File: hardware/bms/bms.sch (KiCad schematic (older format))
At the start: 172 parts

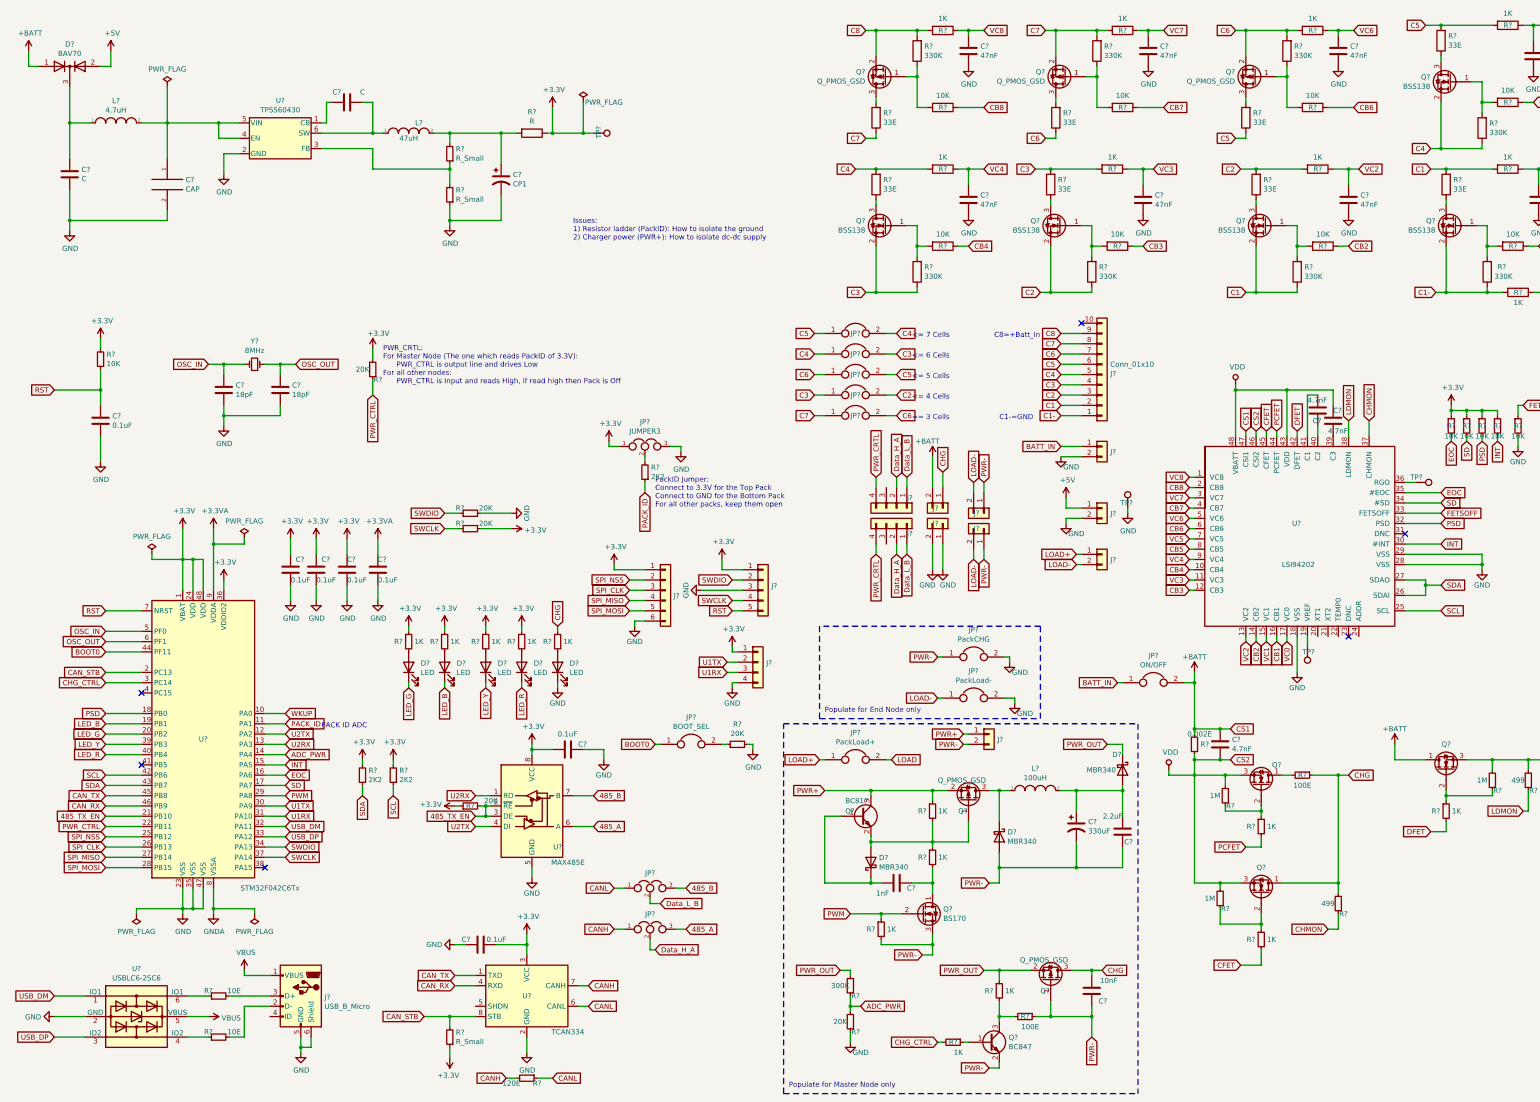
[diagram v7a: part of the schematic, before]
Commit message: added pack power management
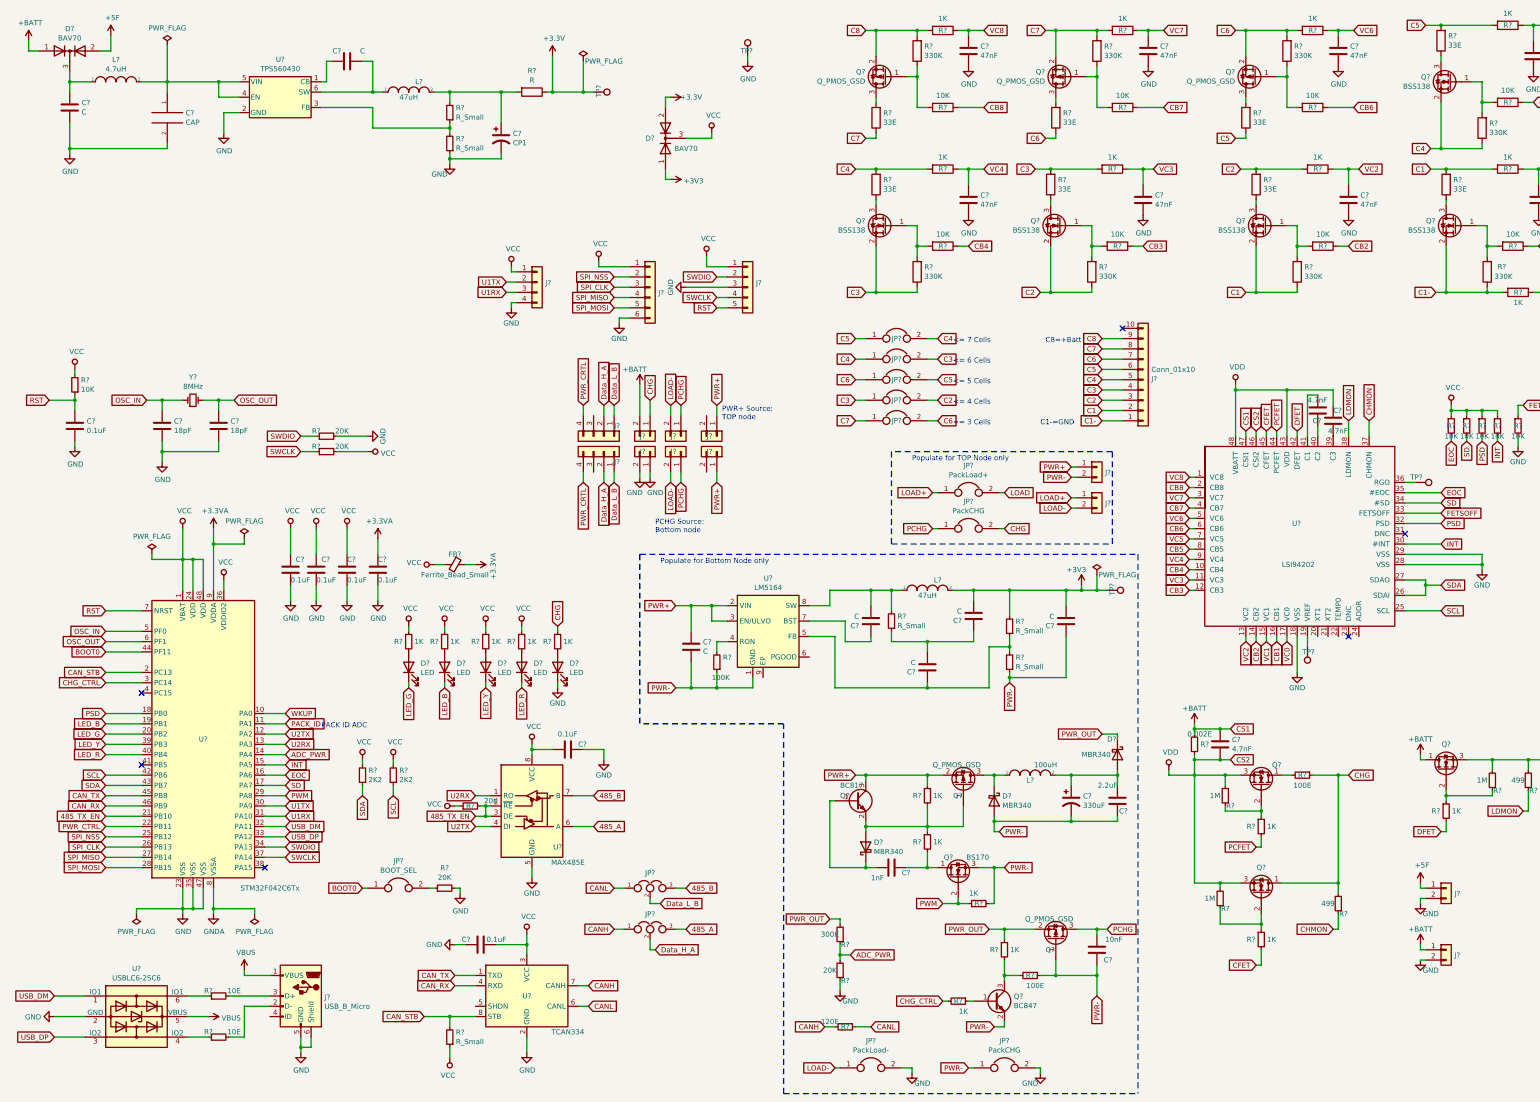
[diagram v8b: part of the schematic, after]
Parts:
- removed JP?: JUMPER3, symbol BMS:JUMPER3
- removed JP?: ON/OFF, symbol BMS:JUMPER
- removed R?: 2K2, Resistor_SMD:R_0603_1608Metric_Pad1.05x0.95mm_HandSolder, symbol Device:R_Small
- removed R?: 20K, Resistor_SMD:R_0603_1608Metric_Pad1.05x0.95mm_HandSolder, symbol Device:R_Small
- added C? (x5): C, Capacitor_SMD:C_0603_1608Metric_Pad1.05x0.95mm_HandSolder, symbol Device:C
- added D?: BAV70, Package_TO_SOT_SMD:SOT-23, symbol Diode:BAV70
- added FB?: Ferrite_Bead_Small, symbol Device:Ferrite_Bead_Small
- added J? (x2): Conn_01x02, symbol BMS:Conn_01x02
- added JP?: PackCHG, symbol BMS:JUMPER
- added L?: 47uH, Inductor_SMD:L_Bourns_SRN6045TA, symbol pspice:INDUCTOR
- added R?: 100K, Resistor_SMD:R_0603_1608Metric_Pad1.05x0.95mm_HandSolder, symbol Device:R_Small
- added R? (x3): R_Small, Resistor_SMD:R_0603_1608Metric_Pad1.05x0.95mm_HandSolder, symbol Device:R_Small
- added TP?: TestPoint, symbol Connector:TestPoint
- added U?: LM5164, Package_SO:SOIC-8-1EP_3.9x4.9mm_P1.27mm_EP2.95x4.9mm_Mask2.71x3.4mm_ThermalVias, symbol BMS:LM5164
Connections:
- net BATT_IN is gone; now on net +BATT: J?.1 (Pin_1)
- net +3.3VA: now also FB?.1
- net +3V3: now also C?.2, C?.2, D?.1 (A), D?.2 (A), L?.2, R?.2, TP?.1; no longer C?.1, C?.1, C?.1, C?.2, C?.2, J?.1 (Pin_1), J?.1 (Pin_1), J?.1 (Pin_1), R?.1, R?.1, R?.1, R?.1, R?.1, R?.1, R?.1, R?.1, R?.1, R?.1, R?.2, R?.2, R?.2, R?.2, U?.1 (VBAT), U?.24 (VDD), U?.3 (VCC), U?.36 (VDDIO2), U?.48 (VDD), U?.8 (VCC)
- net CHG: now also JP?.2; no longer C?.2, Q?.3 (D)
- net PWR+: now also C?.1, J?.1 (Pin_1), J?.1 (Pin_1), U?.2 (VIN), U?.3 (EN/ULVO)
- net PWR-: now also C?.1, C?.2, R?.1, R?.1, U?.1 (GND); no longer J?.1 (Pin_1), J?.1 (Pin_1)
- net +5V renamed +5F
- new net: R?.2, U?.4 (RON)
- new net: C?.1, R?.1, R?.2, U?.5 (FB)
- new net: C?.1, U?.7 (BST)
- new net: C?.2, L?.1, R?.2, U?.8 (SW)
- new net: C?.1, C?.2, R?.1
- new net PCHG: C?.2, J?.1 (Pin_1), J?.1 (Pin_1), JP?.1, Q?.3 (D)
- new net VCC: C?.1, C?.1, C?.1, C?.2, C?.2, D?.3 (K), FB?.2, J?.1 (Pin_1), J?.1 (Pin_1), J?.1 (Pin_1), R?.1, R?.1, R?.1, R?.1, R?.1, R?.1, R?.1, R?.1, R?.1, R?.1, R?.2, R?.2, R?.2, R?.2, U?.1 (VBAT), U?.24 (VDD), U?.3 (VCC), U?.36 (VDDIO2), U?.48 (VDD), U?.8 (VCC)
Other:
- note added: "C8=+Batt"
- note added: "PCHG Source:\nBottom node"
- note added: "PWR+ Source:\nTOP node"
- note added: "Populate for Bottom Node only"
- note added: "Populate for TOP Node only"
- note removed: "C8=+Batt_In"
- note removed: "Issues:\n1) Resistor ladder (PackID): How to isolate the ground\n2) Charger power (PWR+): How to isolate dc-dc supply"
- note removed: "PWR_CRTL:\nFor Master Node (The one which reads PackID of 3.3V):\n PWR_CTRL is output line and drives Low\nFor all other nodes:\n PWR_CTRL is Input and reads High, if read high then Pack is Off"
- note removed: "PackID Jumper:\nConnect to 3.3V for the Top Pack\nConnect to GND for the Bottom Pack\nFor all other packs, keep them open"
- note removed: "Populate for End Node only"
- note removed: "Populate for Master Node only"
- moved on the sheet: C?, D?, J?, JP?, L?, Q?, R?, TP?, U?, Y?
